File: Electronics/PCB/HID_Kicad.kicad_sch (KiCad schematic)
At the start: 7 parts, among them J1_encoder1 Conn_01x05_Male, J2_Switches1 Conn_01x05_Male

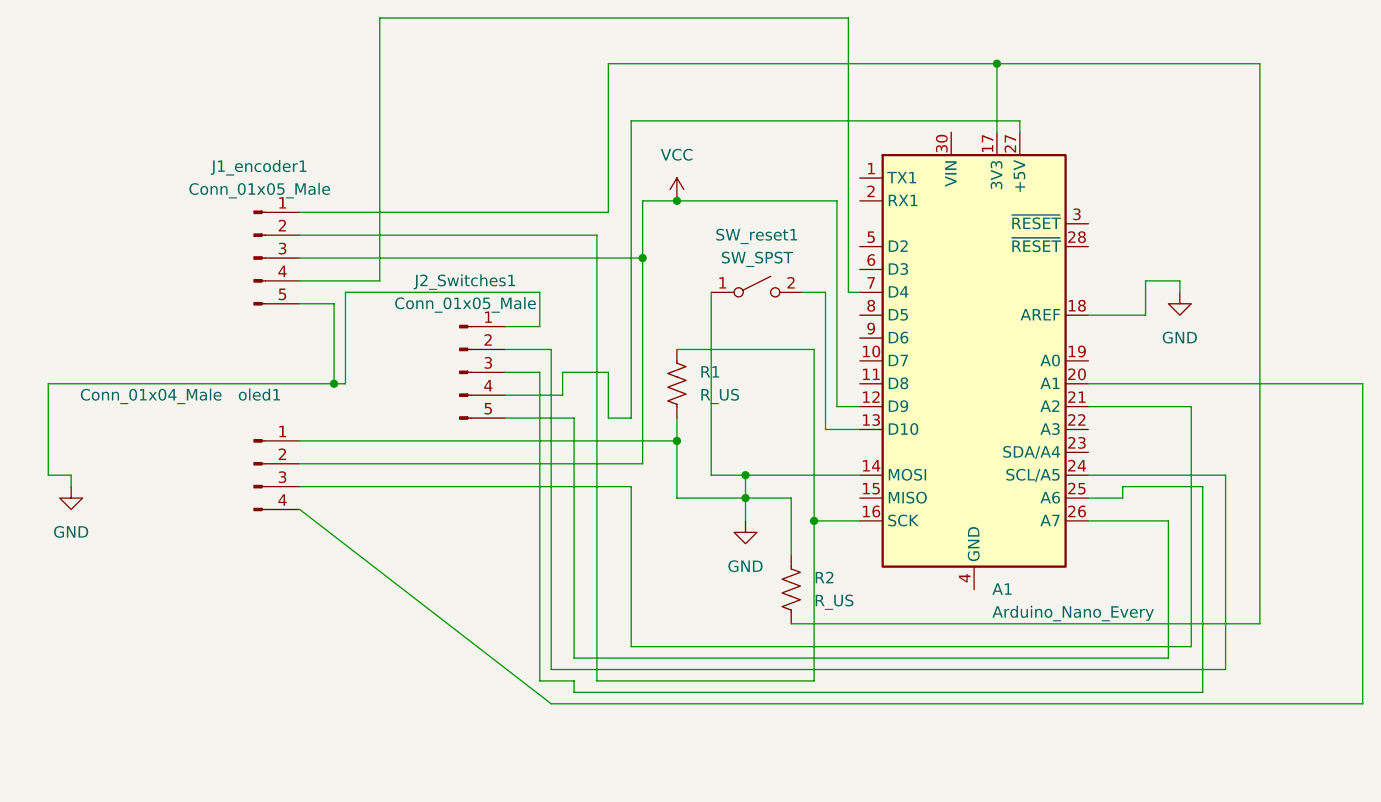
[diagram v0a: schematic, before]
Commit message: updated pcb layout, added vcc for switches
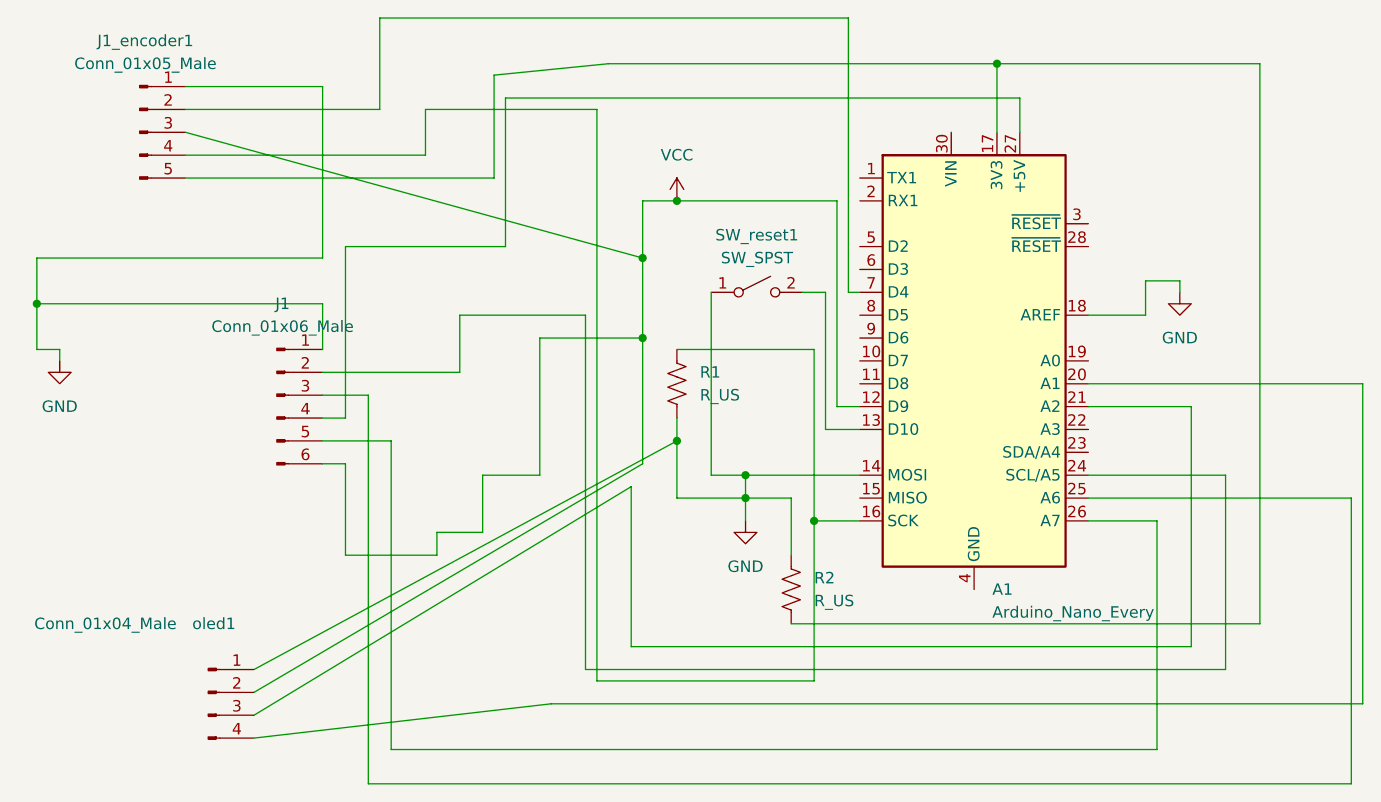
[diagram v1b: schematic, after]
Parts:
- removed J2_Switches1: Conn_01x05_Male, Connector_Wire:SolderWire-0.5sqmm_1x05_P4.8mm_D0.9mm_OD2.3mm, symbol Connector:Conn_01x05_Male
- added J1: Conn_01x06_Male, Connector_Wire:SolderWire-0.5sqmm_1x06_P4.8mm_D0.9mm_OD2.3mm, symbol Connector:Conn_01x06_Male
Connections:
- net GND: now also J1_encoder1.1 (Pin_1), J1.1 (Pin_1); no longer J1_encoder1.5 (Pin_5)
- net VCC: now also J1.6 (Pin_6)
- net at A1.16 (SCK), R1.1: now also J1_encoder1.4 (Pin_4); no longer J1_encoder1.2 (Pin_2)
- net at A1.17 (3V3), R2.2: now also J1_encoder1.5 (Pin_5); no longer J1_encoder1.1 (Pin_1)
- net at A1.24 (SCL/A5): now also J1.2 (Pin_2)
- net at A1.25 (A6): now also J1.3 (Pin_3)
- net at A1.26 (A7): now also J1.5 (Pin_5)
- net at A1.27 (+5V): now also J1.4 (Pin_4)
- net at A1.7 (D4): now also J1_encoder1.2 (Pin_2); no longer J1_encoder1.4 (Pin_4)
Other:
- moved on the sheet: J1_encoder1, oled1

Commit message: PCB design updated to fit inside enclosure
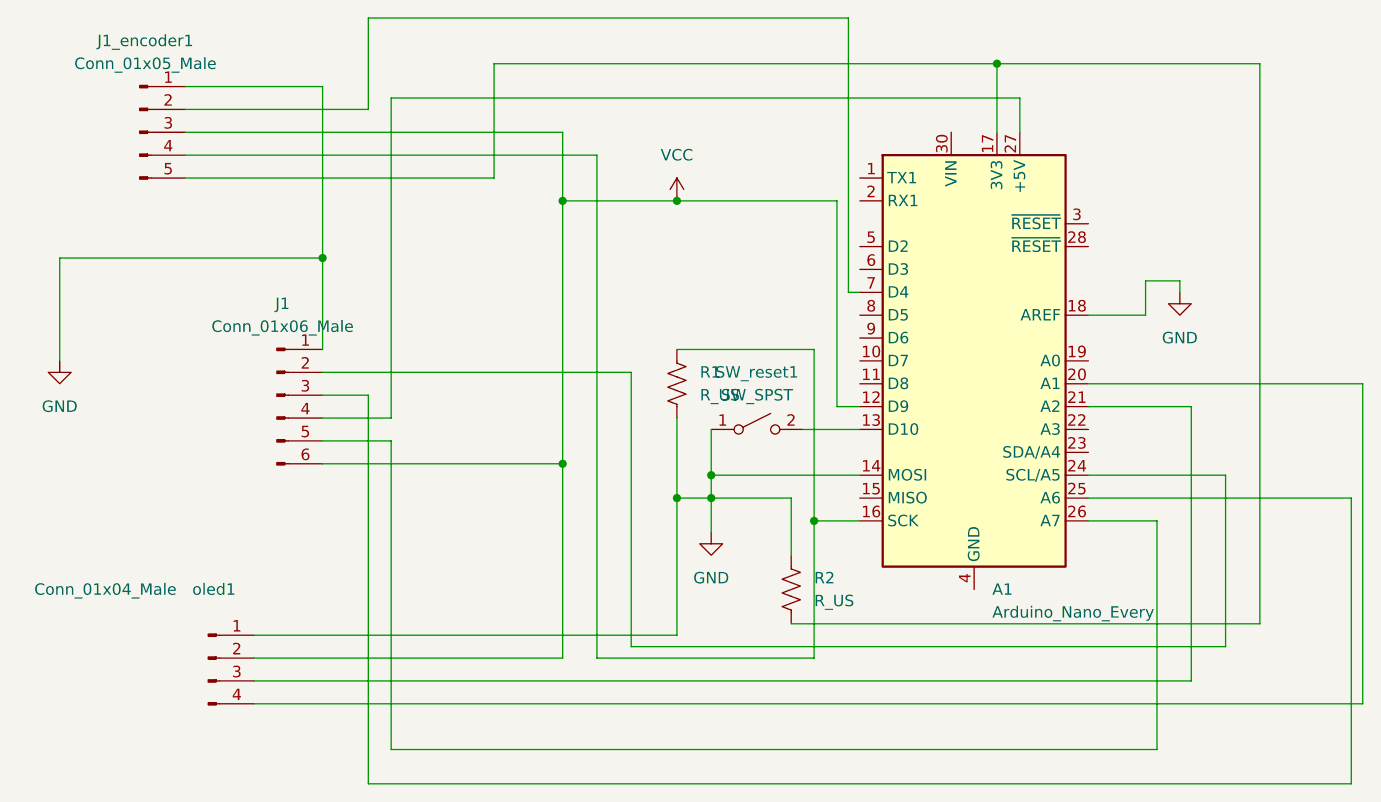
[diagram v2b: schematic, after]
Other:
- moved on the sheet: SW_reset1, oled1
